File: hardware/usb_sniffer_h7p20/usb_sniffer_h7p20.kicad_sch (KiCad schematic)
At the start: 98 parts, among them J1 FPGA_JTAG, J4 USB_C_Receptacle_USB2.0_16P, J5 FFC-40P-0.5mm,NC, U1 H7P20N0L128-M3H1, U6 P25Q32SH-SSH-IT, U7 CY7C68013A-56LTX, U8 24C64BN, U9 CJ3439KDW, X1 XO32,26M,NC, Y2 24M

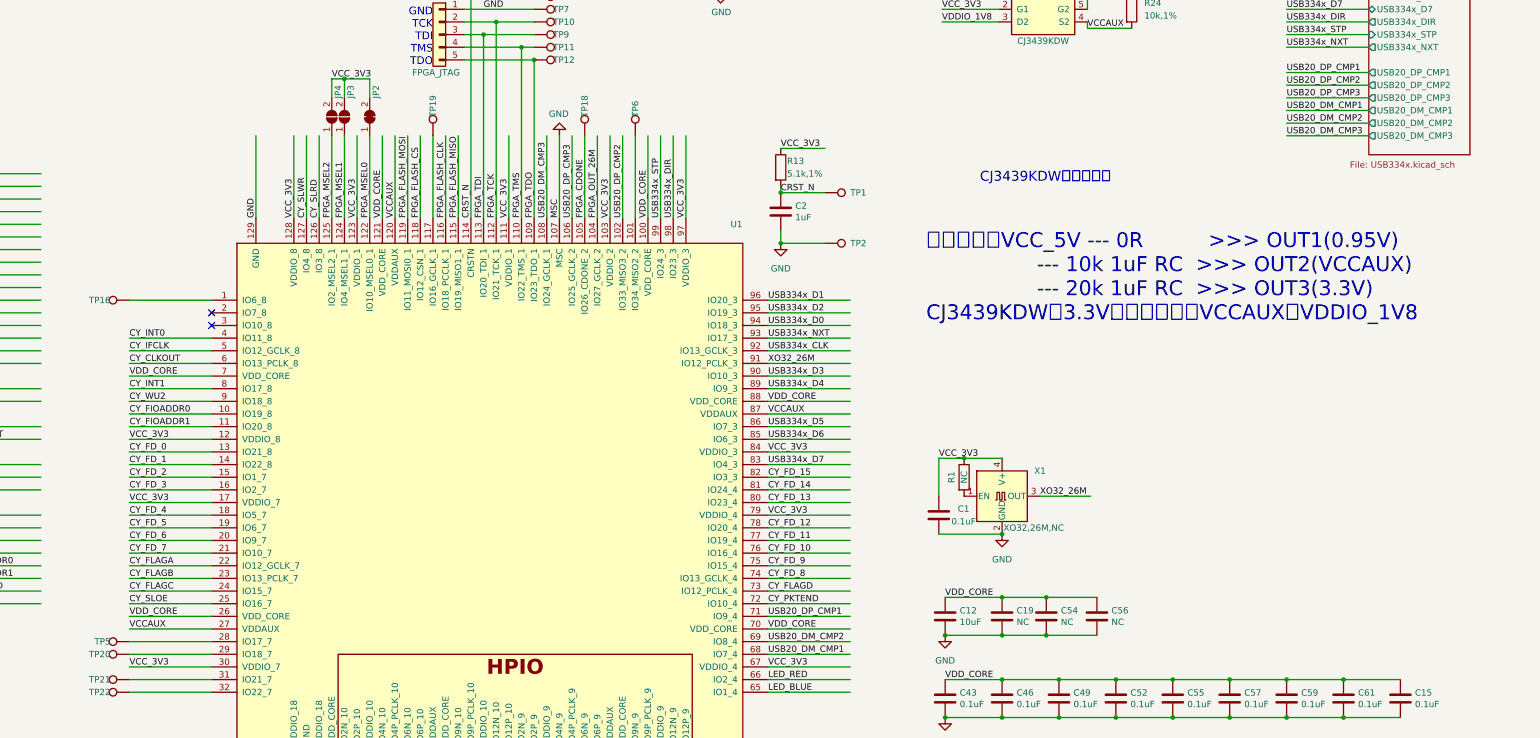
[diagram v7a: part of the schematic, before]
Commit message: [usb_sniffer_h7p20] 预留外部触发接口，优化布局，支持M4隔离柱
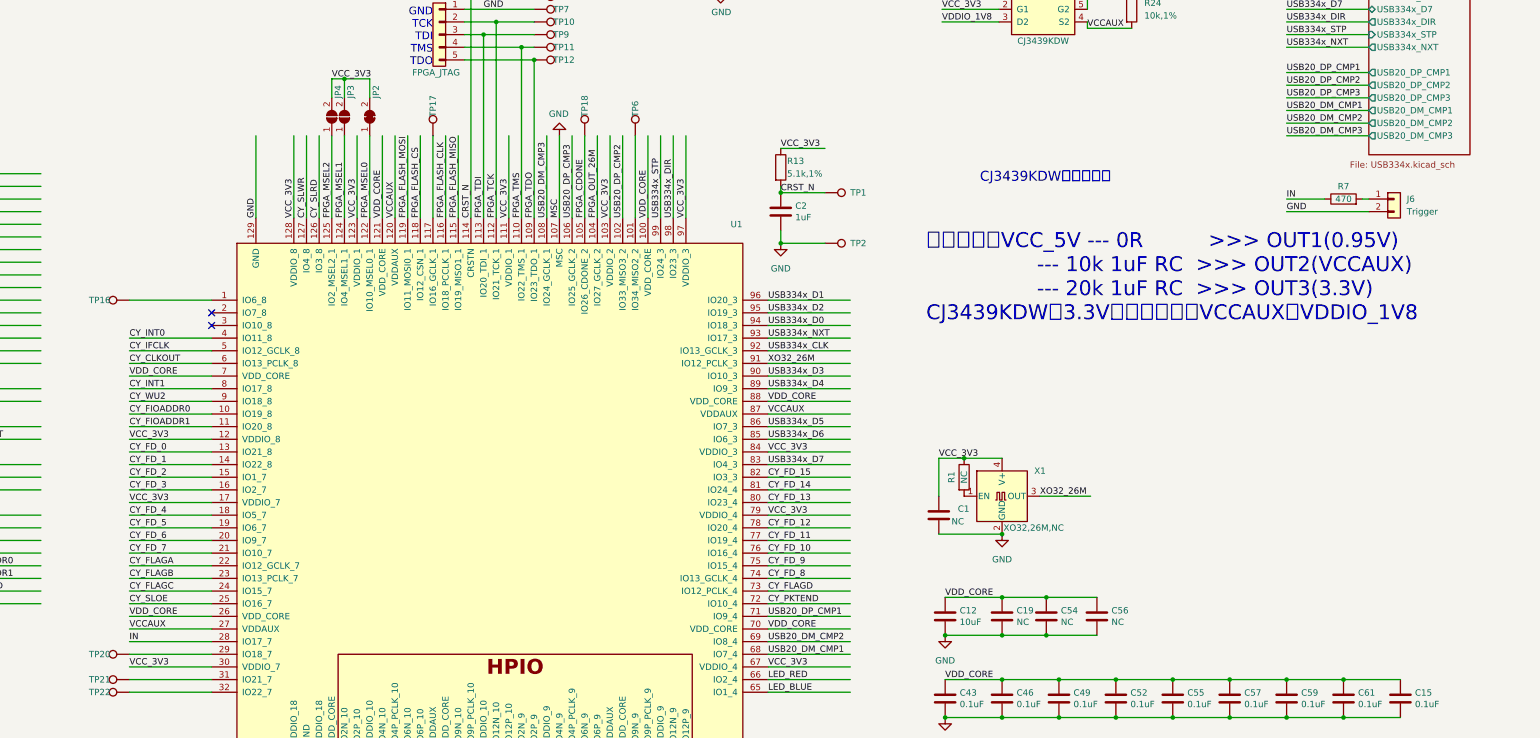
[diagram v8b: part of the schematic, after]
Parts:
- removed TP19, TP5: TestPoint, vllogic:TestPoint_Pad_D0.3mm, symbol Connector:TestPoint
- added J6: Trigger, Connector_PinHeader_2.54mm:PinHeader_1x02_P2.54mm_Vertical, symbol Connector_Generic:Conn_01x02
- added R7: 470, Resistor_SMD:R_0402_1005Metric, symbol Device:R
- added TP17: TestPoint, vllogic:TestPoint_Pad_D0.3mm, symbol Connector:TestPoint
- C1: value 0.1uF -> NC
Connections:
- net GND: now also J6.2 (Pin_2)
- net IN: now reaches U1.28 (IO17_7)
- net IN: now also R7.1
- net at U1.117 (IO16_GCLK_1): now also TP17.1
- new net: J6.1 (Pin_1), R7.2
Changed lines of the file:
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@@
     (stroke (width 0) (type default))
   )
+  (wire (pts (xy 350.52 95.25) (xy 367.03 95.25))
+    (stroke (width 0) (type default))
+  )
   (wire (pts (xy 310.515 52.07) (xy 310.515 54.61))
     (stroke (width 0) (type default))
@@
     (stroke (width 0) (type default))
   )
+  (wire (pts (xy 365.76 92.71) (xy 367.03 92.71))
+    (stroke (width 0) (type default))
+  )
   (wire (pts (xy 114.3 30.48) (xy 118.11 30.48))
     (stroke (width 0) (type default))
@@
     (stroke (width 0) (type default))
   )
+  (wire (pts (xy 350.52 92.71) (xy 358.14 92.71))
+    (stroke (width 0) (type default))
+  )
   (wire (pts (xy 262.89 123.19) (xy 246.38 123.19))
     (stroke (width 0) (type default))
@@
     (effects (font (size 1.27 1.27)) (justify left bottom))
   )
+  (label "GND" (at 350.52 95.25 0) (fields_autoplaced)
+    (effects (font (size 1.27 1.27)) (justify left bottom))
+  )
   (label "CY_INT0" (at 82.55 156.21 0) (fields_autoplaced)
     (effects (font (size 1.27 1.27)) (justify left bottom))
@@
     (effects (font (size 1.27 1.27)) (justify left bottom))
   )
+  (label "IN" (at 118.11 181.61 0) (fields_autoplaced)
+    (effects (font (size 1.27 1.27)) (justify left bottom))
+  )
   (label "B9_IO9P" (at 222.25 224.79 90) (fields_autoplaced)
     (effects (font (size 1.27 1.27)) (justify left bottom))
@@
     (effects (font (size 1.27 1.27)) (justify left bottom))
   )
+  (label "IN" (at 350.52 92.71 0) (fields_autoplaced)
+    (effects (font (size 1.27 1.27)) (justify left bottom))
+  )
   (label "B10_IO9N" (at 170.18 246.38 90) (fields_autoplaced)
     (effects (font (size 1.27 1.27)) (justify left bottom))
@@
     )
   )
-  (symbol (lib_id "Connector:TestPoint") (at 118.11 181.61 90) (unit 1)
-    (in_bom yes) (on_board yes) (dnp no)
-    (property "Reference" "TP5" (at 114.3 181.61 90)
-      (effects (font (size 1.27 1.27)) (justify left))
-    )
-    (property "Value" "TestPoint" (at 113.03 180.34 90)
-      (effects (font (size 1.27 1.27)) (justify left) hide)
-    )
-    (property "Footprint" "vllogic:TestPoint_Pad_D0.3mm" (at 118.11 176.53 0)
-      (effects (font (size 1.27 1.27)) hide)
-    )
-    (property "Datasheet" "~" (at 118.11 176.53 0)
-      (effects (font (size 1.27 1.27)) hide)
-    )
-    (pin "1")
-    (instances
-      (project "usb_sniffer_h7p20"
-        (path "/5a8287a8-9f7a-4e60-a3bf-19c1227b20fe"
-          (reference "TP5") (unit 1)
-        )
-      )
-    )
-  )
   (symbol (lib_id "Device:C") (at 33.02 194.31 180) (unit 1)
     (in_bom yes) (on_board yes) (dnp no)
@@
       (effects (font (size 1.27 1.27)) (justify right))
     )
-    (property "Value" "0.1uF" (at 283.21 157.48 0)
+    (property "Value" "NC" (at 283.21 157.48 0)
       (effects (font (size 1.27 1.27)) (justify right))
     )
@@
     )
   )
+  (symbol (lib_id "Connector:TestPoint") (at 179.07 80.01 0) (unit 1)
+    (in_bom yes) (on_board yes) (dnp no)
+    (property "Reference" "TP17" (at 179.07 76.2 90)
+      (effects (font (size 1.27 1.27)) (justify left))
+    )
+    (property "Value" "TestPoint" (at 180.34 74.93 90)
+      (effects (font (size 1.27 1.27)) (justify left) hide)
+    )
+    (property "Footprint" "vllogic:TestPoint_Pad_D0.3mm" (at 184.15 80.01 0)
+      (effects (font (size 1.27 1.27)) hide)
+    )
+    (property "Datasheet" "~" (at 184.15 80.01 0)
+      (effects (font (size 1.27 1.27)) hide)
+    )
+    (pin "1")
+    (instances
+      (project "usb_sniffer_h7p20"
+        (path "/5a8287a8-9f7a-4e60-a3bf-19c1227b20fe"
+          (reference "TP17") (unit 1)
+        )
+      )
+    )
+  )
   (symbol (lib_id "Device:Crystal_GND24_Small") (at 31.75 88.9 0) (unit 1)
     (in_bom yes) (on_board yes) (dnp no)
@@
     )
   )
+  (symbol (lib_id "Device:R") (at 361.95 92.71 90) (unit 1)
+    (in_bom yes) (on_board yes) (dnp no)
+    (property "Reference" "R7" (at 361.95 90.17 90)
+      (effects (font (size 1.27 1.27)))
+    )
+    (property "Value" "470" (at 361.95 92.71 90)
+      (effects (font (size 1.27 1.27)))
+    )
+    (property "Footprint" "Resistor_SMD:R_0402_1005Metric" (at 361.95 94.488 90)
+      (effects (font (size 1.27 1.27)) hide)
+    )
+    (property "Datasheet" "~" (at 361.95 92.71 0)
+      (effects (font (size 1.27 1.27)) hide)
+    )
+    (pin "2")
+    (pin "1")
+    (instances
+      (project "usb_sniffer_h7p20"
+        (path "/5a8287a8-9f7a-4e60-a3bf-19c1227b20fe"
+          (reference "R7") (unit 1)
+        )
+      )
+    )
+  )
   (symbol (lib_id "Connector:TestPoint") (at 40.64 120.65 0) (unit 1)
     (in_bom yes) (on_board yes) (dnp no)
@@
     )
   )
+  (symbol (lib_id "Connector_Generic:Conn_01x02") (at 372.11 92.71 0) (unit 1)
+    (in_bom yes) (on_board yes) (dnp no) (fields_autoplaced)
+    (property "Reference" "J6" (at 374.65 92.71 0)
+      (effects (font (size 1.27 1.27)) (justify left))
+    )
+    (property "Value" "Trigger" (at 374.65 95.25 0)
+      (effects (font (size 1.27 1.27)) (justify left))
+    )
+    (property "Footprint" "Connector_PinHeader_2.54mm:PinHeader_1x02_P2.54mm_Vertical" (at 372.11 92.71 0)
+      (effects (font (size 1.27 1.27)) hide)
+    )
+    (property "Datasheet" "~" (at 372.11 92.71 0)
+      (effects (font (size 1.27 1.27)) hide)
+    )
+    (pin "2")
+    (pin "1")
+    (instances
+      (project "usb_sniffer_h7p20"
+        (path "/5a8287a8-9f7a-4e60-a3bf-19c1227b20fe"
+          (reference "J6") (unit 1)
+        )
+      )
+    )
+  )
   (symbol (lib_id "Device:C") (at 293.37 209.55 180) (unit 1)
     (in_bom yes) (on_board yes) (dnp no)
@@
         )
       )
-    )
-  )
-  (symbol (lib_id "Connector:TestPoint") (at 179.07 80.01 0) (unit 1)
-    (in_bom yes) (on_board yes) (dnp no)
-    (property "Reference" "TP19" (at 179.07 76.2 90)
-      (effects (font (size 1.27 1.27)) (justify left))
-    )
-    (property "Value" "TestPoint" (at 180.34 74.93 90)
-      (effects (font (size 1.27 1.27)) (justify left) hide)
-    )
-    (property "Footprint" "vllogic:TestPoint_Pad_D0.3mm" (at 184.15 80.01 0)
-      (effects (font (size 1.27 1.27)) hide)
-    )
-    (property "Datasheet" "~" (at 184.15 80.01 0)
-      (effects (font (size 1.27 1.27)) hide)
-    )
-    (pin "1")
-    (instances
-      (project "usb_sniffer_h7p20"
-        (path "/5a8287a8-9f7a-4e60-a3bf-19c1227b20fe"
-          (reference "TP19") (unit 1)
-        )
-      )
